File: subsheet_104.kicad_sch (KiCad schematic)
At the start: 8 parts

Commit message: ports d'extension et cartouche
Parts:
- added B01: Connecteur extension (dessous), symbol Connector_Generic:Conn_01x19
- added B02: Connecteur extension (dessus), symbol Connector_Generic:Conn_01x19
- added B06: Port cartouche (rangée 'a' vers le sud), symbol Connector_Generic:Conn_02x15_Row_Letter_First
- added ZW02: TestPoint, symbol Connector:TestPoint
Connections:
- net +5V: now also B02.19 (Pin_19), B06.b2 (Pin_b2)
- net GND: now also B01.2 (Pin_2), B02.1 (Pin_1), B06.b14 (Pin_b14)
- new net: B01.1 (Pin_1), ZW02.1
- new net A0: B02.16 (Pin_16), B06.a14 (Pin_a14)
- new net A1: B02.15 (Pin_15), B06.a13 (Pin_a13)
- new net A10: B02.6 (Pin_6), B06.a4 (Pin_a4)
- new net A11: B02.5 (Pin_5), B06.a3 (Pin_a3)
- new net A12: B06.a2 (Pin_a2)
- new net A13: B06.b4 (Pin_b4)
- new net A14: B06.b1 (Pin_b1)
- new net A15: B06.a1 (Pin_a1)
- new net A2: B02.14 (Pin_14), B06.a12 (Pin_a12)
- new net A3: B02.13 (Pin_13), B06.a11 (Pin_a11)
- new net A4: B02.12 (Pin_12), B06.a10 (Pin_a10)
- new net A5: B02.11 (Pin_11), B06.a9 (Pin_a9)
- new net A6: B02.10 (Pin_10), B06.a8 (Pin_a8)
- new net A7: B02.9 (Pin_9), B06.a7 (Pin_a7)
- new net A8: B02.8 (Pin_8), B06.a6 (Pin_a6)
- new net A9: B02.7 (Pin_7), B06.a5 (Pin_a5)
- new net A/SYNLT: B02.18 (Pin_18)
- new net B/NBXXX: B02.17 (Pin_17)
- new net C/NAXXX: B02.4 (Pin_4)
- new net D0: B01.13 (Pin_13), B06.b13 (Pin_b13)
- new net D1: B01.12 (Pin_12), B06.b12 (Pin_b12)
- new net D2: B01.11 (Pin_11), B06.b11 (Pin_b11)
- new net D3: B01.10 (Pin_10), B06.b10 (Pin_b10)
- new net D4: B01.9 (Pin_9), B06.b9 (Pin_b9)
- new net D5: B01.8 (Pin_8), B06.b8 (Pin_b8)
- new net D6: B01.7 (Pin_7), B06.b7 (Pin_b7)
- new net D7: B01.6 (Pin_6), B06.b6 (Pin_b6)
- new net D/NA7CX: B02.3 (Pin_3)
- new net E: B01.5 (Pin_5)
- new net E/CLRG: B02.2 (Pin_2)
- new net F/VIDEO: B01.18 (Pin_18)
- new net G/~{IRQ}: B01.17 (Pin_17)
- new net H/VCO-16MHz: B01.16 (Pin_16)
- new net I/~{FIRQ}: B01.15 (Pin_15)
- new net J/~{RESET}: B01.14 (Pin_14)
- new net K/SON: B01.3 (Pin_3)
- new net L/CSCART: B06.b5 (Pin_b5)
- new net M/PRCART: B06.b3 (Pin_b3)
- new net R/~{W}: B01.4 (Pin_4)
- no-connect marks 0 -> 3
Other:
- note added: "De I29"
- note added: "Les broches 1 sont à gauche"
- note added: "Pour la compatibilité avec l'extension 64K Nanoréseau - Lier la broche a15 à R/~{W} - Lier la broche b15 à E Référence : https://forum.system-cfg.com/viewtopic.php?p=229228#p229228"
- note added: "Vers C17 (mélangeur audio LEP)"
- note added: "Vers I46"

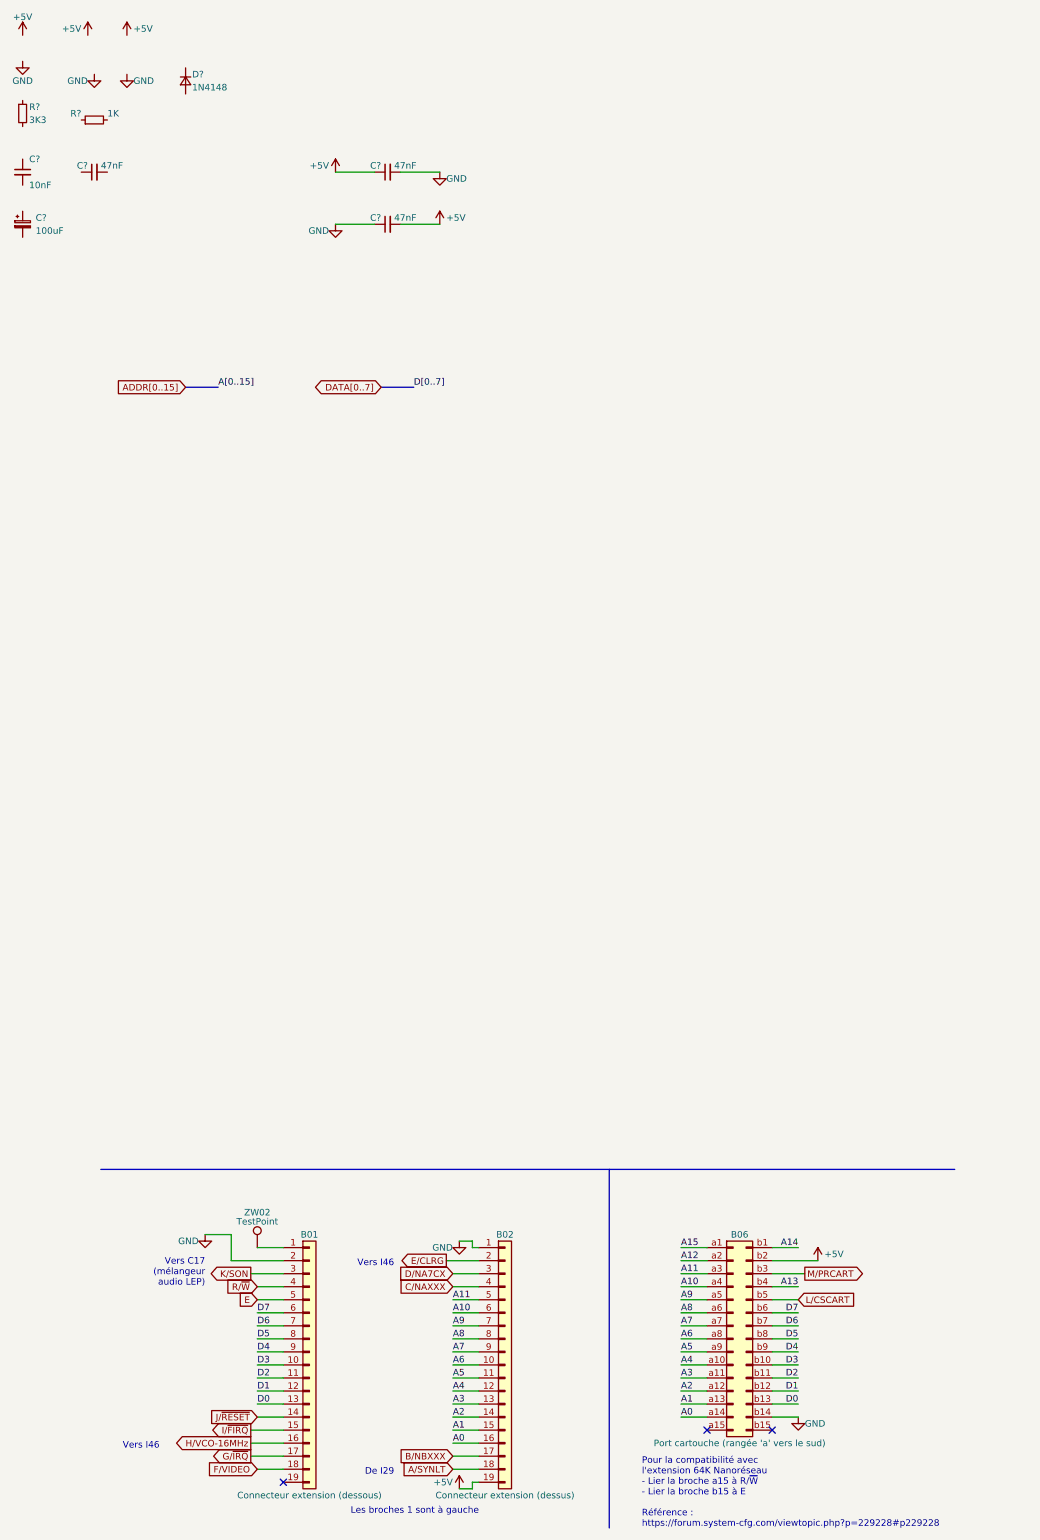
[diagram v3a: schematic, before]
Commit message: decodage d'addresse, re-pagination
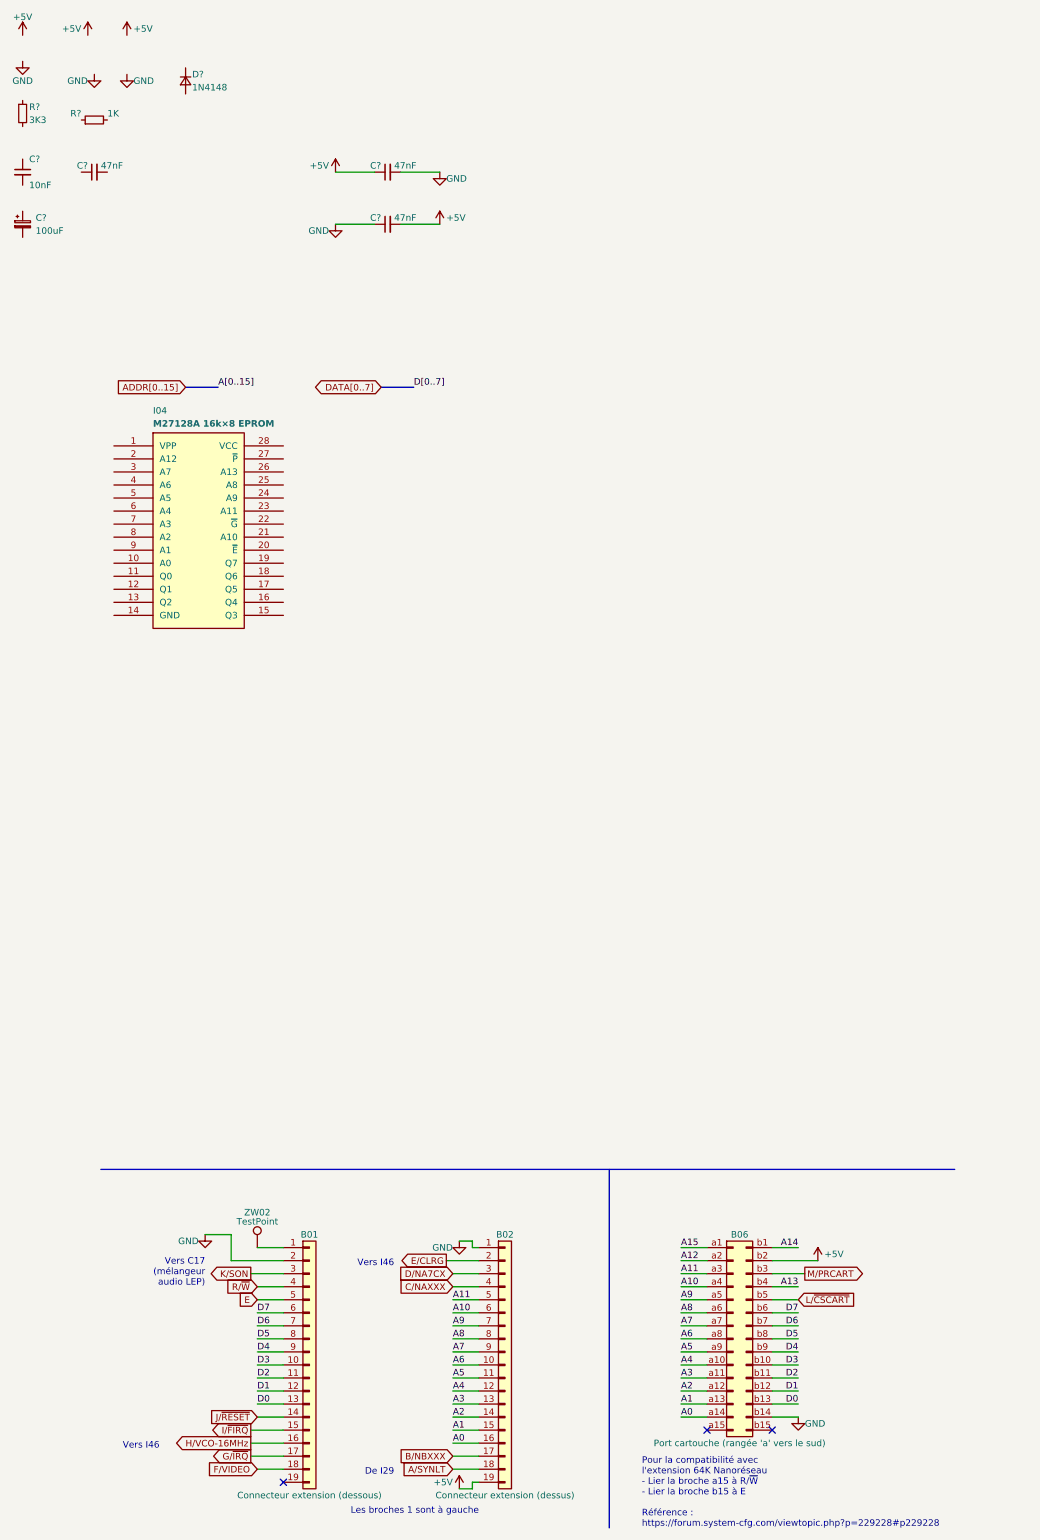
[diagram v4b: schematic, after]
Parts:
- added I04: M27128A 16k×8 EPROM, Package_DIP:DIP-28_W15.24mm_LongPads, symbol 27128:M27128A_NMOS_128K_16K_X_8_UV_EPROM_PHY
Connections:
- net L/CSCART renamed L/~{CSCART}
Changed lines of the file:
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@@
   (title_block
     (title "Conversion du Thomson MO5 — Unité centrale v1")
-    (date "2023-05-21")
+    (date "2023-05-24")
     (rev "DRAFT")
     (comment 1 "http://github.com/sporniket/kicad-conversions--thomson-mo5--v1")
@@
     )
   )
-  (global_label "L{slash}CSCART" (shape input) (at 157.48 203.2 0) (fields_autoplaced)
+  (global_label "L{slash}~{CSCART}" (shape input) (at 157.48 203.2 0) (fields_autoplaced)
     (effects (font (size 1.27 1.27)) (justify left))
     (property "Intersheet References" "${INTERSHEET_REFS}" (id 0) (at 169.3274 203.1206 0)
@@
     (pin "2")
   )
+  (symbol (lib_id "27128:M27128A_NMOS_128K_16K_X_8_UV_EPROM_PHY") (at 40.64 53.34 0) (unit 1)
+    (in_bom yes) (on_board yes)
+    (property "Reference" "I04" (id 0) (at 31.75 29.21 0)
+      (effects (font (size 1.27 1.27)) (justify left top))
+    )
+    (property "Value" "M27128A 16k×8 EPROM" (id 1) (at 31.75 31.75 0)
+      (effects (font (size 1.27 1.27) bold) (justify left top))
+    )
+    (property "Footprint" "Package_DIP:DIP-28_W15.24mm_LongPads" (id 2) (at 31.75 26.67 0)
+      (effects (font (size 1.27 1.27)) (justify left top) hide)
+    )
+    (property "Datasheet" "https://pdf.datasheetcatalog.com/datasheet_pdf/sgs-thomson-microelectronics/27128.pdf" (id 3) (at 31.75 24.13 0)
+      (effects (font (size 1.27 1.27)) (justify left top) hide)
+    )
+    (pin "1")
+    (pin "10")
+    (pin "11")
+    (pin "12")
+    (pin "13")
+    (pin "14")
+    (pin "15")
+    (pin "16")
+    (pin "17")
+    (pin "18")
+    (pin "19")
+    (pin "2")
+    (pin "20")
+    (pin "21")
+    (pin "22")
+    (pin "23")
+    (pin "24")
+    (pin "25")
+    (pin "26")
+    (pin "27")
+    (pin "28")
+    (pin "3")
+    (pin "4")
+    (pin "5")
+    (pin "6")
+    (pin "7")
+    (pin "8")
+    (pin "9")
+  )
   (symbol (lib_id "power:+5V") (at 6.35 -43.18 0) (unit 1)

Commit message: fini eprom, réarrange la feuille, version alpha
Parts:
- removed C?: 10nF, symbol Device:C_Small
- removed C? (x3): 47nF, symbol Device:C_Small
- removed C?: 100uF, symbol Device:C_Polarized_Small
- removed D?: 1N4148, symbol Device:D_Small
- removed R?: 1K, symbol Device:R_Small
- removed R?: 3K3, symbol Device:R_Small
- added C25: 47nF, symbol Device:C_Small
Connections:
- net +5V: now also I04.1 (VPP), I04.27 (~{P}), I04.28 (VCC), C25.2
- net A0: now also I04.10 (A0)
- net A1: now also I04.9 (A1)
- net A10: now also I04.21 (A10)
- net A11: now also I04.23 (A11)
- net A12: now also I04.2 (A12)
- net A13: now also I04.26 (A13)
- net A2: now also I04.8 (A2)
- net A3: now also I04.7 (A3)
- net A4: now also I04.6 (A4)
- net A5: now also I04.5 (A5)
- net A6: now also I04.4 (A6)
- net A7: now also I04.3 (A7)
- net A8: now also I04.25 (A8)
- net A9: now also I04.24 (A9)
- net D0: now also I04.11 (Q0)
- net D1: now also I04.12 (Q1)
- net D2: now also I04.13 (Q2)
- net D3: now also I04.15 (Q3)
- net D4: now also I04.16 (Q4)
- net D5: now also I04.17 (Q5)
- net D6: now also I04.18 (Q6)
- net D7: now also I04.19 (Q7)
- net GND: now also I04.14 (GND), C25.1
- net ~{CS_EPROM}: now reaches I04.20 (~{E})
- net ~{CS_EPROM}: now also I04.22 (~{G})
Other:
- moved on the sheet: B01, B02, B06, I04, ZW02
